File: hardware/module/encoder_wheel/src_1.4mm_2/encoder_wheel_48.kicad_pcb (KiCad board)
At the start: 2 copper layers, 74 x 74 mm, 2 parts

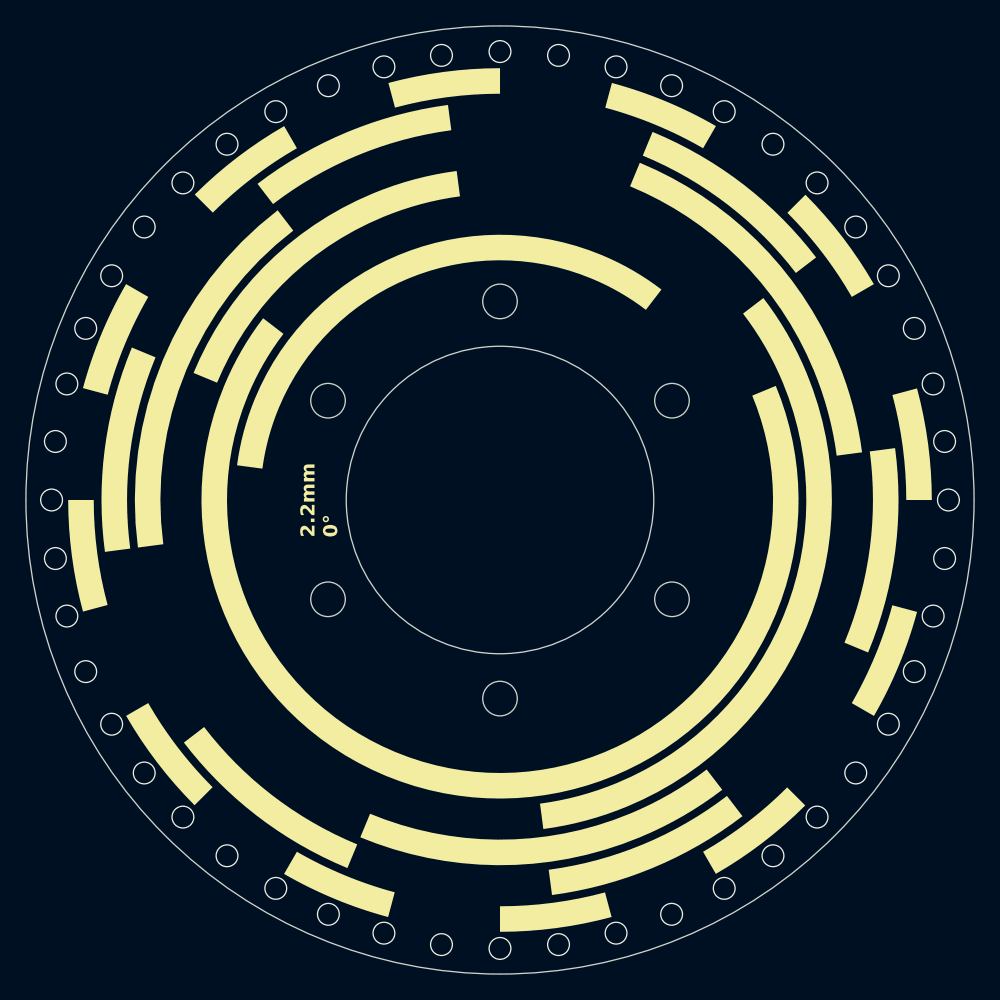
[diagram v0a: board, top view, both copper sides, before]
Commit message: add encoder wheel variants
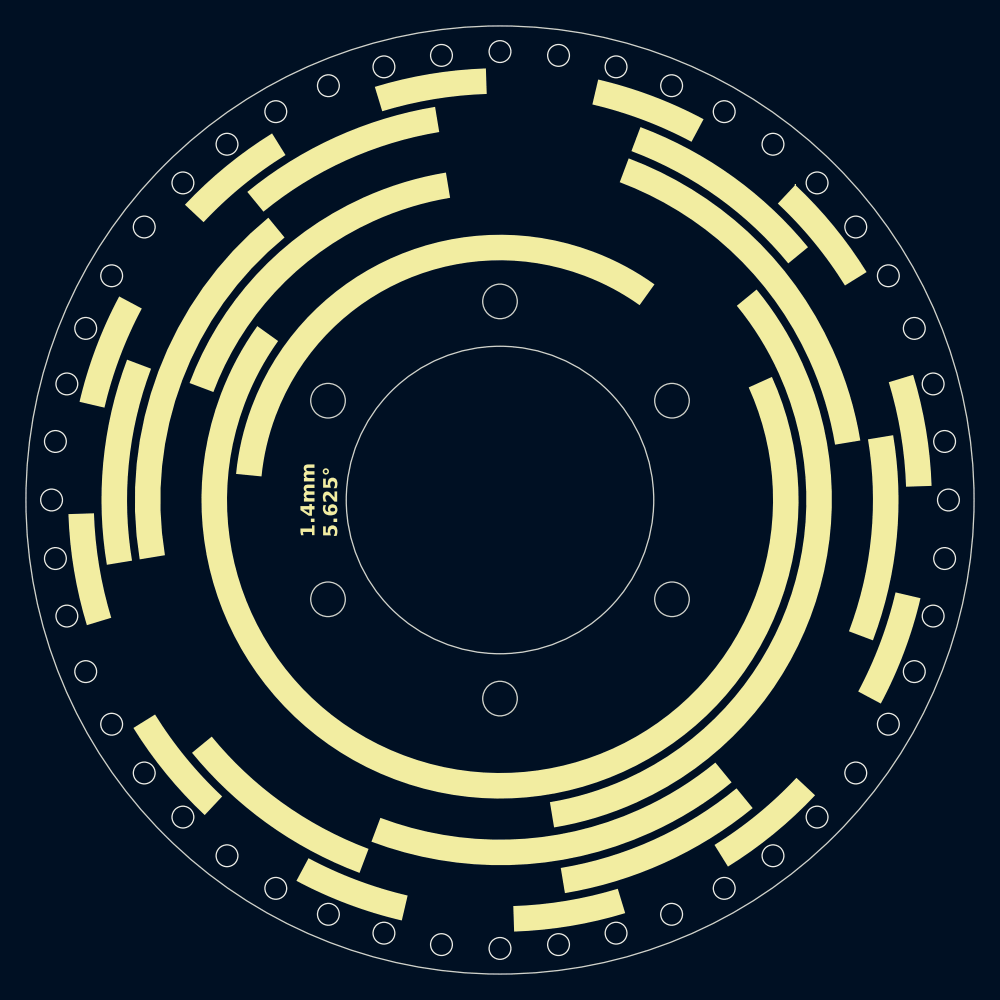
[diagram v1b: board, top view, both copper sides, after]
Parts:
- REF** (x2): value OpenFlapEncoderPattern48_2.2mm -> OpenFlapEncoderPattern48_1.4mm; footprint EncoderPattern:OpenFlapEncoderPattern48_2.2mm -> EncoderPattern:OpenFlapEncoderPattern48_1.4mm
- turned REF** to 1.875 degrees
- turned REF** to -178.125 degrees
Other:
- board text added: "1.4mm 1.875°"
- board text added: "1.4mm 5.625°"
- board text removed: "2.2mm 0°"
- board text removed: "2.2mm 3.75°"

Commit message: encoder changes
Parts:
- renumbered REF** to ENC1, REF** to ENC2

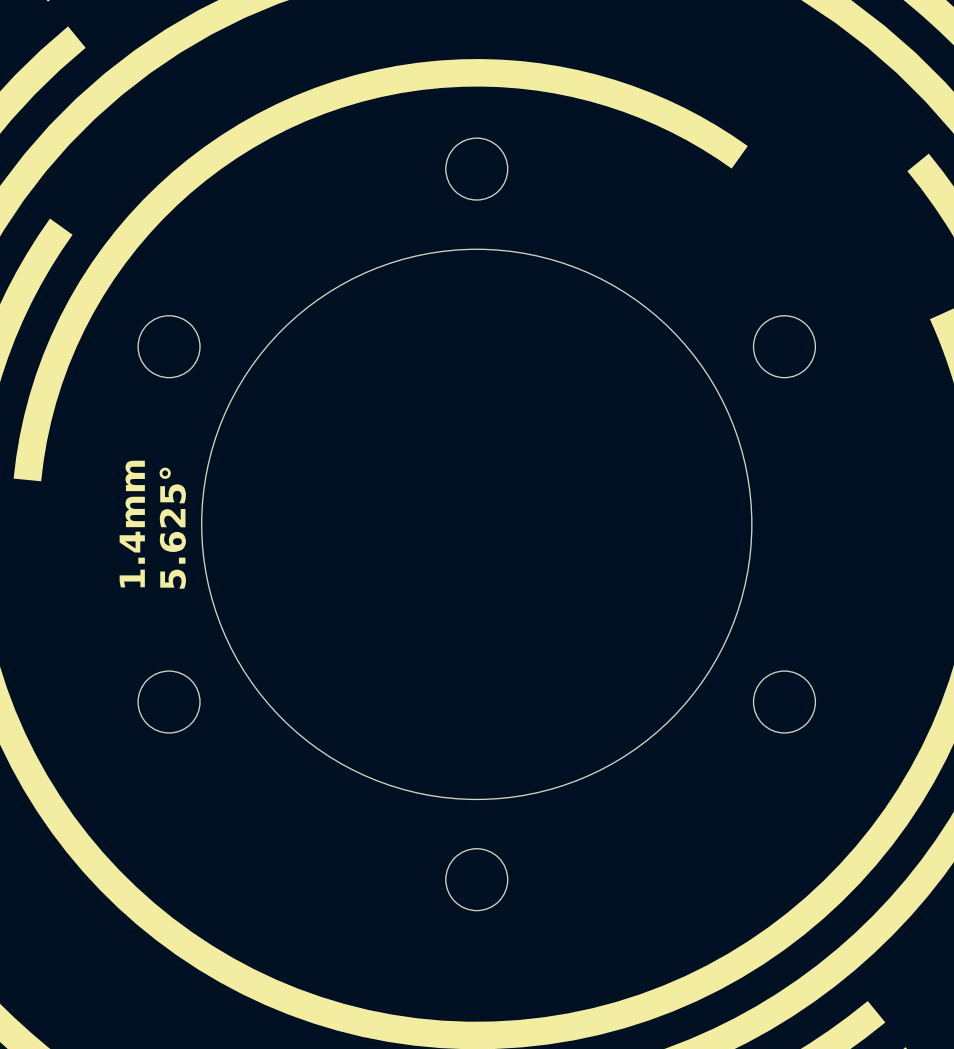
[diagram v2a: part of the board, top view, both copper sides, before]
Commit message: changed hole patern encoder wheel
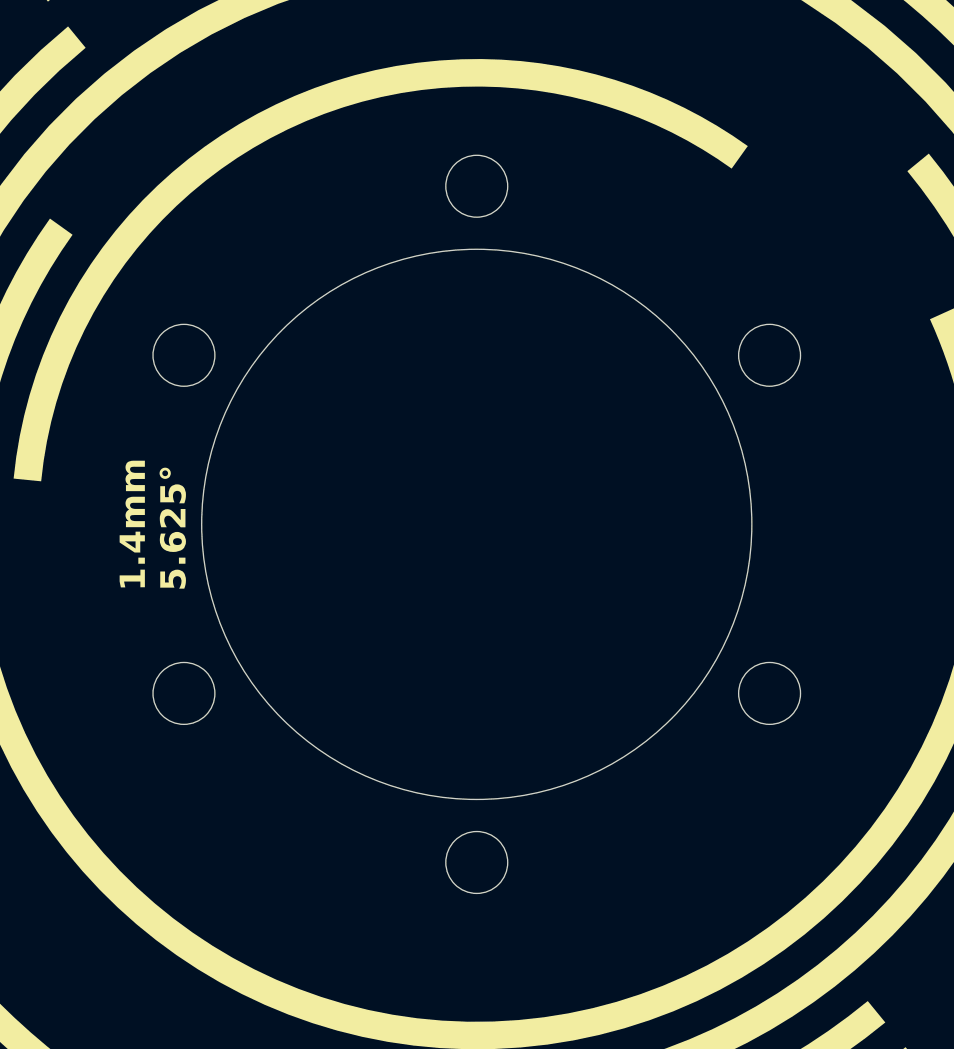
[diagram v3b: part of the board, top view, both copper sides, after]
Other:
- outline, holes or cut-outs redrawn
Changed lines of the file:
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@@
 				(xy 30.762689 12.77682) (xy 30.329678 13.773227) (xy 29.865412 14.752395) (xy 29.370483 15.713684)
 				(xy 28.845481 16.656453) (xy 27.799552 16.052353) (xy 28.306017 15.143779) (xy 28.783494 14.217412)
-				(xy 29.231411 13.273868) (xy 29.649198 12.313758) (xy 30.036284 11.337709) (xy 30.392098 10.346323)
+				(xy 29.231411 13.273868) (xy 29.649198 12.313756) (xy 30.036284 11.337709) (xy 30.392098 10.346323)
 				(xy 30.71607 9.340219) (xy 31.007628 8.320012)
 			)
@@
 		(fp_poly
 			(pts
-				(xy 0.001769 -32.099226) (xy 0.000217 -32.099226) (xy -1.07175 -32.081547) (xy -2.134858 -32.028909)
+				(xy 0.001769 -32.099226) (xy 0.000217 -32.099226) (xy -1.07175 -32.081547) (xy -2.134856 -32.028909)
 				(xy -3.188601 -31.941911) (xy -4.232446 -31.821152) (xy -5.265878 -31.66723) (xy -6.288377 -31.480743)
 				(xy -7.299424 -31.26229) (xy -8.298499 -31.012471) (xy -8.610108 -32.17519) (xy -7.573698 -32.433874)
@@
 			(pts
 				(xy 24.313345 -22.761289) (xy 25.043118 -21.956167) (xy 25.746626 -21.127422) (xy 26.423221 -20.27572)
-				(xy 27.072257 -19.40172) (xy 27.693088 -18.506101) (xy 28.285067 -17.589513) (xy 28.847549 -16.652624)
+				(xy 27.072257 -19.401718) (xy 27.693088 -18.506101) (xy 28.285067 -17.589513) (xy 28.847549 -16.652624)
 				(xy 27.801101 -16.049043) (xy 27.533521 -16.502718) (xy 27.258776 -16.9516) (xy 26.976942 -17.395607)
 				(xy 26.688094 -17.83466) (xy 26.392309 -18.268676) (xy 26.089664 -18.697577) (xy 25.780236 -19.121279)
@@
 				(xy -17.205855 23.958074) (xy -16.414609 24.50821) (xy -15.604859 25.032894) (xy -14.777186 25.531546)
 				(xy -13.932167 26.003588) (xy -13.070383 26.448439) (xy -12.192411 26.865519) (xy -11.298833 27.25425)
-				(xy -11.759793 28.366845) (xy -12.690463 27.962615) (xy -13.604831 27.528858) (xy -14.50229 27.066174)
+				(xy -11.759795 28.366845) (xy -12.690463 27.962615) (xy -13.604831 27.528858) (xy -14.50229 27.066174)
 				(xy -15.382238 26.575165) (xy -16.244074 26.056432) (xy -17.087198 25.510575) (xy -17.911007 24.938197)
 				(xy -18.714901 24.339898) (xy -19.498278 23.716279) (xy -20.260538 23.067942) (xy -21.001078 22.395488)
-				(xy -21.719298 21.699518) (xy -22.414597 20.980633) (xy -23.086372 20.239435) (xy -23.734029 19.476524)
+				(xy -21.719298 21.699518) (xy -22.414597 20.980633) (xy -23.086372 20.239435) (xy -23.734031 19.476524)
 				(xy -24.356951 18.692502) (xy -23.398869 17.957146)
 			)
@@
 				(xy -16.372943 -21.337093) (xy -17.545687 -20.382265) (xy -18.662484 -19.364281) (xy -19.720615 -18.285856)
 				(xy -20.71736 -17.149698) (xy -21.649997 -15.958522) (xy -22.515808 -14.715038) (xy -23.31207 -13.421959)
-				(xy -24.036065 -12.081996) (xy -24.685077 -10.697861) (xy -25.25637 -9.272266) (xy -25.74724 -7.807923)
+				(xy -24.036065 -12.081996) (xy -24.685079 -10.697861) (xy -25.25637 -9.272266) (xy -25.74724 -7.807923)
 				(xy -26.15496 -6.307543) (xy -26.476812 -4.773838) (xy -26.710073 -3.209521) (xy -26.852025 -1.617303)
 				(xy -26.899947 0.000104) (xy -26.896307 0.444588) (xy -26.885437 0.887331) (xy -26.867412 1.32828)
@@
 				(xy 28.602175 7.243801) (xy 28.769784 6.545229) (xy 28.9207 5.840342) (xy 29.054699 5.129358) (xy 29.171558 4.412495)
 				(xy 29.271053 3.689973) (xy 29.352959 2.962008) (xy 29.417054 2.228821) (xy 29.463112 1.490629)
-				(xy 29.490912 0.74765) (xy 29.500228 0.000104) (xy 29.496225 -0.487345) (xy 29.484275 -0.972866)
+				(xy 29.490912 0.74765) (xy 29.500228 0.000104) (xy 29.496225 -0.487343) (xy 29.484275 -0.972866)
 				(xy 29.464466 -1.456396) (xy 29.436887 -1.937891) (xy 29.401625 -2.417303) (xy 29.358768 -2.894584)
 				(xy 29.308406 -3.369684) (xy 29.250625 -3.842555) (xy 30.440734 -3.999652)
@@
 				(xy -9.925757 -16.315126) (xy -10.638275 -15.858129) (xy -11.328794 -15.370896) (xy -11.996379 -14.854365)
 				(xy -12.640096 -14.309472) (xy -13.25901 -13.737156) (xy -13.852187 -13.138354) (xy -14.418693 -12.514003)
-				(xy -14.957592 -11.86504) (xy -15.46795 -11.192402) (xy -15.948833 -10.497028) (xy -16.399306 -9.779849)
+				(xy -14.957592 -11.86504) (xy -15.46795 -11.192402) (xy -15.948833 -10.497028) (xy -16.399306 -9.779847)
 				(xy -16.818435 -9.041817) (xy -17.205285 -8.283856) (xy -17.558921 -7.506907) (xy -17.87841 -6.711908)
-				(xy -18.162816 -5.899791) (xy -18.411205 -5.071508) (xy -18.622642 -4.227982) (xy -18.796194 -3.370156)
+				(xy -18.162816 -5.899789) (xy -18.411205 -5.071508) (xy -18.622642 -4.227982) (xy -18.796194 -3.370156)
 				(xy -18.930924 -2.498966) (xy -20.127751 -2.657096) (xy -19.984916 -3.584168) (xy -19.800829 -4.496891)
 				(xy -19.576478 -5.394275) (xy -19.312853 -6.275331) (xy -19.010942 -7.139071) (xy -18.671733 -7.984505)
@@
 				(xy 24.194689 2.286607) (xy 24.274268 1.150209) (xy 24.301059 0.000104) (xy 24.27925 -1.037404)
 				(xy 24.214407 -2.063841) (xy 24.10741 -3.078336) (xy 23.959134 -4.080021) (xy 23.770459 -5.068026)
-				(xy 23.542261 -6.041486) (xy 23.275419 -6.999517) (xy 22.97081 -7.941265) (xy 22.629311 -8.865855)
+				(xy 23.542261 -6.041487) (xy 23.275419 -6.999517) (xy 22.97081 -7.941265) (xy 22.629311 -8.865855)
 				(xy 22.251802 -9.772417) (xy 21.839159 -10.660082) (xy 21.392259 -11.527981) (xy 20.911982 -12.375244)
 				(xy 20.399204 -13.201002) (xy 19.854804 -14.004384) (xy 19.279658 -14.784522) (xy 20.238257 -15.519361)
@@
 				(xy -9.931567 20.643658) (xy -10.919046 20.13818) (xy -11.878054 19.587018) (xy -12.807158 18.991607)
 				(xy -13.704923 18.353381) (xy -14.569914 17.673775) (xy -15.400696 16.954222) (xy -16.195837 16.196159)
-				(xy -16.953901 15.401018) (xy -17.673453 14.570236) (xy -18.353054 13.705245) (xy -18.991285 12.80748)
+				(xy -16.953901 15.401018) (xy -17.673453 14.570236) (xy -18.353052 13.705245) (xy -18.991285 12.80748)
 				(xy -19.586696 11.878376) (xy -20.137858 10.919368) (xy -20.643337 9.931889) (xy -21.101697 8.917374)
 				(xy -21.511504 7.877259) (xy -21.871325 6.812976) (xy -22.179724 5.725961) (xy -22.435268 4.617647)
@@
 				(xy 9.690245 31.86793) (xy 10.734594 31.532185) (xy 11.763622 31.163388) (xy 12.776691 30.76214)
 				(xy 13.77316 30.329041) (xy 14.752389 29.864692) (xy 15.713738 29.369693) (xy 16.656566 28.844645)
-				(xy 16.051951 27.798714) (xy 15.14342 28.305174) (xy 14.217106 28.782699) (xy 13.273635 29.230701)
+				(xy 16.051951 27.798714) (xy 15.14342 28.305174) (xy 14.217104 28.782699) (xy 13.273635 29.230701)
 				(xy 12.313603 29.648592) (xy 11.337624 30.035786) (xy 10.346311 30.391694) (xy 9.340275 30.715729)
 				(xy 8.320125 31.007303) (xy 8.631217 32.170023)
@@
 			(pts
 				(xy 23.543483 -23.557839) (xy 22.76267 -24.313192) (xy 21.957549 -25.0429) (xy 21.12879 -25.746324)
-				(xy 20.277067 -26.422829) (xy 19.403052 -27.071773) (xy 18.507418 -27.692535) (xy 17.590836 -28.284462)
+				(xy 20.277067 -26.422829) (xy 19.403052 -27.071771) (xy 18.507418 -27.692535) (xy 17.590836 -28.284462)
 				(xy 16.653979 -28.846924) (xy 16.049884 -27.800988) (xy 16.503537 -27.533413) (xy 16.952405 -27.258669)
 				(xy 17.396405 -26.976833) (xy 17.835456 -26.687982) (xy 18.269475 -26.392193) (xy 18.698382 -26.089542)
@@
 				(xy 28.901689 -10.378028) (xy 28.644365 -11.068655) (xy 28.371093 -11.751324) (xy 27.258498 -11.290371)
 				(xy 27.521566 -10.63428) (xy 27.769284 -9.970563) (xy 28.001427 -9.299438) (xy 28.217773 -8.621124)
-				(xy 28.418096 -7.935838) (xy 28.60218 -7.243801) (xy 28.769784 -6.545229) (xy 28.9207 -5.840342)
+				(xy 28.418096 -7.935838) (xy 28.602182 -7.243801) (xy 28.769784 -6.545229) (xy 28.9207 -5.840342)
 				(xy 29.054699 -5.129358) (xy 29.171558 -4.412495) (xy 29.271053 -3.689973) (xy 29.352959 -2.962008)
 				(xy 29.417054 -2.228821) (xy 29.463112 -1.490629) (xy 29.490912 -0.74765) (xy 29.500228 -0.000104)
@@
 				(xy -5.564034 -27.548968) (xy -6.235452 -27.405542) (xy -6.900826 -27.246247) (xy -7.559953 -27.071293)
 				(xy -8.212626 -26.880893) (xy -8.858641 -26.675258) (xy -9.497792 -26.4546) (xy -10.129874 -26.21913)
-				(xy -10.754682 -25.969064) (xy -10.293727 -24.856469) (xy -9.695495 -25.096342) (xy -9.090321 -25.322225)
+				(xy -10.754682 -25.969066) (xy -10.293727 -24.856469) (xy -9.695495 -25.096342) (xy -9.090321 -25.322225)
 				(xy -8.478403 -25.533911) (xy -7.859938 -25.731196) (xy -7.235124 -25.913876) (xy -6.60416 -26.081744)
 				(xy -5.967244 -26.234598) (xy -5.324572 -26.372231) (xy -4.676344 -26.494439) (xy -4.022757 -26.601017)
@@
 	)
 	(gr_circle
-		(center 87.576606 107.75)
-		(end 88.926606 107.75)
+		(center 88.226125 107.375)
+		(end 89.576125 107.375)
 		(stroke
 			(width 0.05)
@@
 	)
 	(gr_circle
-		(center 101 84.5)
-		(end 102.35 84.5)
+		(center 101 85.25)
+		(end 102.35 85.25)
 		(stroke
 			(width 0.05)
@@
 	)
 	(gr_circle
-		(center 114.423394 92.25)
-		(end 115.773394 92.25)
+		(center 113.773875 92.625)
+		(end 115.123875 92.625)
 		(stroke
 			(width 0.05)
@@
 	)
 	(gr_circle
-		(center 87.576606 92.25)
-		(end 88.926606 92.25)
+		(center 88.226125 92.625)
+		(end 89.576125 92.625)
 		(stroke
 			(width 0.05)
@@
 	)
 	(gr_circle
-		(center 114.423394 107.75)
-		(end 115.773394 107.75)
+		(center 113.773875 107.375)
+		(end 115.123875 107.375)
 		(stroke
 			(width 0.05)
@@
 	)
 	(gr_circle
-		(center 101 115.5)
-		(end 102.35 115.5)
+		(center 101 114.75)
+		(end 102.35 114.75)
 		(stroke
 			(width 0.05)
